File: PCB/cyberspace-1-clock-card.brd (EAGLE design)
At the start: 100 x 50 mm, 40 parts, among them U1 555, U2 Quad AND Gate, U3 Quad AND Gate, U4 QUAD NAND Gate, U5 SCHMIDT INVERTER, U6 HCT32, X1 1-14MHz

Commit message: Clock Card final?
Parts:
- added LOGO1: (no value), gfx-glyphs:SOZU-20MM
- added LOGO2: (no value), gfx-glyphs:CHRONOS2-20MM
- R13: value 1K -> 2K
- U2, U3: value Quad AND Gate -> HCT08
- U4: value QUAD NAND Gate -> HCT00
- U5: value SCHMIDT INVERTER -> HCT14
- moved R13 41.4 mm to (47.8, 37.0), turned to 90 degrees
- moved C4 10.7 mm to (32.7, 15.0)
- moved R12 10.7 mm to (54.3, 37.0)
- moved C5 10.1 mm to (52.9, 37.0)
- moved X1 5.21 mm to (55.0, 43.6), turned to 0 degrees
- moved C1 1.89 mm to (37.5, 25.4)
- moved C10 1.89 mm to (67.5, 25.4)
- moved C7 1.89 mm to (7.50, 25.4)
- moved C8 1.89 mm to (22.5, 25.4)
- moved C9 1.89 mm to (52.5, 25.4)
- moved U2 1.60 mm to (14.0, 25.4)
- moved U3 1.60 mm to (29.0, 25.4)
- moved U4 1.60 mm to (44.0, 25.4)
- moved U5 1.60 mm to (59.0, 25.4)
- moved U6 1.60 mm to (74.0, 25.4)
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- renumbered RP1 to SLOW_ADJ
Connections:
- net !CLK_OUT: now also R13.1; no longer CLK.K
- net N$11: now also CLK.K, R13.2; no longer CLK.A, R13.1
- net VCC: now also CLK.A; no longer R13.2
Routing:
- net VCC: track 0.00 -> 197.9 mm, vias 0 -> 17
- net !MODE_SLOW: track 0.00 -> 113.6 mm, vias 0 -> 3
- net !MODE_MAN: track 0.00 -> 103.2 mm, vias 0 -> 3
- net !MODE_FAST: track 0.00 -> 97.0 mm, vias 0 -> 3
- net !BTN_SLOW: track 0.00 -> 94.2 mm, vias 0 -> 2
- net !BTN_FAST: track 0.00 -> 89.4 mm, vias 0 -> 2
- net !BTN_MAN: track 0.00 -> 85.9 mm, vias 0 -> 2
- net CLK_IN_SLOW: track 0.00 -> 68.8 mm, vias 0 -> 1
- net CLK_OUT: track 0.00 -> 63.4 mm, vias 0 -> 2
- net N$11: track 0.00 -> 58.6 mm
- net N$5: track 0.00 -> 51.5 mm, vias 0 -> 1
- net CLK_OUT_MAN: track 0.00 -> 49.9 mm, vias 0 -> 2
- net CLK_IN_FAST: track 0.00 -> 48.7 mm, vias 0 -> 2
- net CLK_OUT_FAST: track 0.00 -> 47.4 mm, vias 0 -> 2
- net CLK_OUT_SLOW: track 0.00 -> 45.9 mm, vias 0 -> 2
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- added copper zone on layer 1, net GND
- added copper zone on layer 16, net GND
- added copper zone on layer 1, net VCC
- added copper zone on layer 16, net VCC
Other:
- board text added: "2023/12"
- board text added: "Circuit Monkey"
- board text added: "Design by"
- board text added: "Multi-Mode System Clock"
- board text added: "Rev. A"
- board text added: "TIME IS ON THE OTHER SIDE"

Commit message: Resistor missing value.
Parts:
- SLOW_ADJ: value (none) -> 1M
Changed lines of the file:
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@@
 <setting verticaltext="up"/>
 </settings>
-<grid distance="0.1" unitdist="mm" unit="mm" style="lines" multiple="1" display="yes" altdistance="5" altunitdist="mil" altunit="mil"/>
+<grid distance="1" unitdist="mm" unit="mm" style="lines" multiple="1" display="yes" altdistance="5" altunitdist="mil" altunit="mil"/>
 <layers>
 <layer number="1" name="Top" color="4" fill="1" visible="yes" active="yes"/>
@@
 <attribute name="VALUE" x="67.246" y="25.4" size="0.2" layer="27" rot="R270" align="center"/>
 </element>
-<element name="SLOW_ADJ" library="rlc" library_urn="urn:adsk.eagle:library:4192893" package="CERMET_MULTI_3006P_THD" package3d_urn="urn:adsk.eagle:package:42461647/1" value="" x="79" y="7.5" smashed="yes">
+<element name="SLOW_ADJ" library="rlc" library_urn="urn:adsk.eagle:library:4192893" package="CERMET_MULTI_3006P_THD" package3d_urn="urn:adsk.eagle:package:42461647/1" value="1M" x="79" y="7.5" smashed="yes">
 <attribute name="COST01" value="2.00" x="79" y="7.5" size="1.778" layer="27" display="off"/>
 <attribute name="COST10" value="1.70" x="79" y="7.5" size="1.778" layer="27" display="off"/>

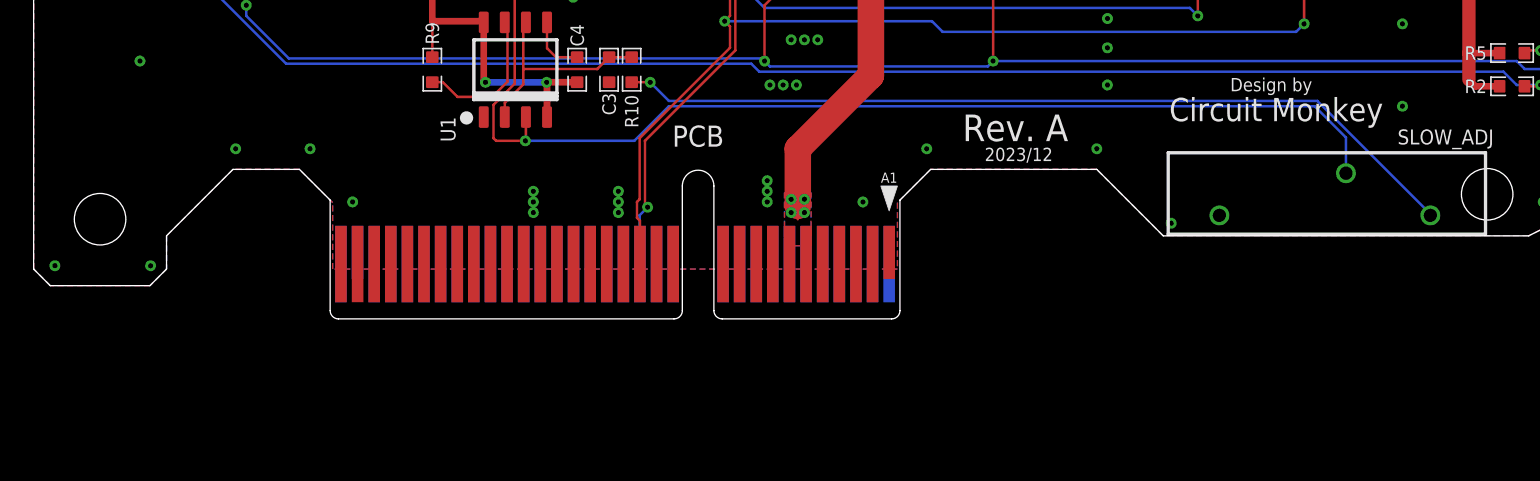
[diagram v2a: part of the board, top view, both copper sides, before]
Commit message: WIP. Proposed clock fix in schematic.
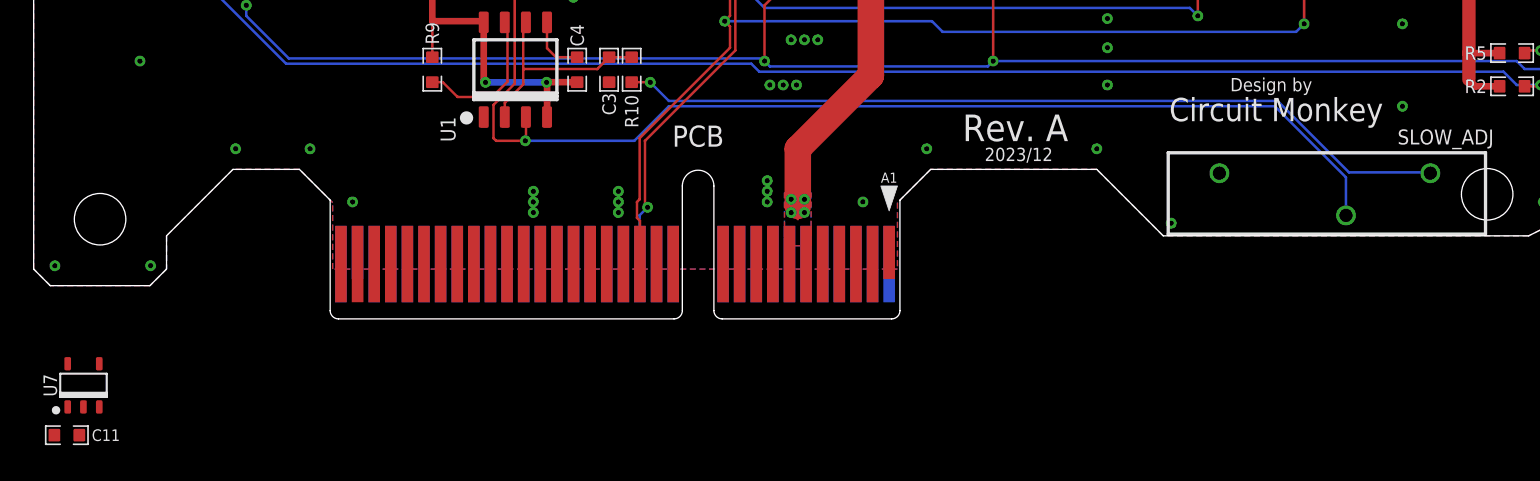
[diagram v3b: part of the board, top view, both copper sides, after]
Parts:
- added C11: 0.1uF, rlc:0603-CAP
- added U7: (no value), logic:TSOP-5
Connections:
- net GND: now also C11.2, U7.3
- net VCC: now also C11.1, U7.5
- net XTAL_IN: now also U7.2
- net XTAL_OUT: now also U7.4
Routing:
- net CLK_IN_SLOW: track 68.8 -> 69.9 mm
- net N$5: track 51.5 -> 50.3 mm
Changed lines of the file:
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@@
 <setting verticaltext="up"/>
 </settings>
-<grid distance="1" unitdist="mm" unit="mm" style="lines" multiple="1" display="yes" altdistance="5" altunitdist="mil" altunit="mil"/>
+<grid distance="0.1" unitdist="mm" unit="mm" style="lines" multiple="1" display="yes" altdistance="5" altunitdist="mil" altunit="mil"/>
 <layers>
 <layer number="1" name="Top" color="4" fill="1" visible="yes" active="yes"/>
@@
 <element name="LOGO1" library="gfx-glyphs" library_urn="urn:adsk.eagle:library:17868973" package="SOZU-20MM" value="" x="32.6" y="40" smashed="yes"/>
 <element name="LOGO2" library="gfx-glyphs" library_urn="urn:adsk.eagle:library:17868973" package="CHRONOS2-20MM" value="" x="73.1" y="38.4" smashed="yes"/>
+<element name="U7" library="logic" library_urn="urn:adsk.eagle:library:8032508" package="TSOP-5" package3d_urn="urn:adsk.eagle:package:8032592/3" value="" x="3" y="-4" smashed="yes">
+<attribute name="COST01" value="0.35" x="3" y="-4" size="1.778" layer="27" display="off"/>
+<attribute name="COST10" value="0.24" x="3" y="-4" size="1.778" layer="27" display="off"/>
+<attribute name="COST100" value="0.12" x="3" y="-4" size="1.778" layer="27" display="off"/>
+<attribute name="MFR" value="Nexperia" x="3" y="-4" size="1.778" layer="27" display="off"/>
+<attribute name="MPN" value="74HCT1G04GV" x="3" y="-4" size="1.778" layer="27" display="off"/>
+<attribute name="NAME" x="1" y="-4" size="0.8128" layer="25" font="vector" ratio="15" rot="R90" align="center"/>
+<attribute name="VALUE" x="3" y="-4" size="0.254" layer="27" font="vector" align="center"/>
+</element>
+<element name="C11" library="rlc" library_urn="urn:adsk.eagle:library:4192893" package="0603-CAP" package3d_urn="urn:adsk.eagle:package:4193021/5" value="0.1uF" x="2" y="-7" smashed="yes">
+<attribute name="COST01" value="0.12" x="2" y="-7" size="1.778" layer="27" display="off"/>
+<attribute name="COST10" value="0.09" x="2" y="-7" size="1.778" layer="27" display="off"/>
+<attribute name="COST100" value="0.05" x="2" y="-7" size="1.778" layer="27" display="off"/>
+<attribute name="NAME" x="3.5" y="-7" size="0.7" layer="25" font="vector" ratio="15" align="center-left"/>
+<attribute name="VALUE" x="2" y="-7.254" size="0.2" layer="27" align="center"/>
+</element>
 </elements>
 <signals>
@@
 <wire x1="52.5" y1="26.151840625" x2="51.351840625" y2="26.151840625" width="0.4" layer="1"/>
 <wire x1="51.351840625" y1="26.151840625" x2="51.2" y2="26" width="0.4" layer="1"/>
+<contactref element="U7" pad="5"/>
+<contactref element="C11" pad="1"/>
+<wire x1="2.05" y1="-2.7" x2="1.248159375" y2="-7" width="0" layer="19" extent="1-1"/>
+<wire x1="24" y1="15.751840625" x2="2.05" y2="-2.7" width="0" layer="19" extent="1-1"/>
 </signal>
 <signal name="GND">
@@
 <via x="64.64" y="16.32" extent="1-16" drill="0.3048"/>
 <via x="64.64" y="14.08" extent="1-16" drill="0.3048"/>
+<contactref element="U7" pad="3"/>
+<contactref element="C11" pad="2"/>
+<wire x1="2.751840625" y1="-7" x2="3.95" y2="-5.3" width="0" layer="19" extent="1-1"/>
+<wire x1="1.28" y1="3.2" x2="3.95" y2="-5.3" width="0" layer="19" extent="1-1"/>
 </signal>
 <signal name="XTAL_IN">
@@
 <wire x1="55.84" y1="32.96" x2="53.6" y2="35.2" width="0.1524" layer="1"/>
 <wire x1="52.9" y1="37.751840625" x2="53.6" y2="37.751840625" width="0.1524" layer="1"/>
+<contactref element="U7" pad="2"/>
+<wire x1="3" y1="-5.3" x2="59" y2="28.3" width="0" layer="19" extent="1-1"/>
 </signal>
 <signal name="XTAL_OUT">
@@
 <wire x1="56" y1="33.28" x2="57.44" y2="33.28" width="0.1524" layer="1"/>
 <wire x1="60.27" y1="28.3" x2="61.54" y2="28.3" width="0.1524" layer="1"/>
+<contactref element="U7" pad="4"/>
+<wire x1="3.95" y1="-2.7" x2="54.3" y2="36.248159375" width="0" layer="19" extent="1-1"/>
 </signal>
 <signal name="N$4">
@@
 <via x="29.6" y="10.72" extent="1-16" drill="0.3048"/>
 <wire x1="36.16" y1="10.72" x2="38.24" y2="12.8" width="0.1524" layer="16"/>
-<wire x1="38.24" y1="12.8" x2="77.12" y2="12.8" width="0.1524" layer="16"/>
+<wire x1="38.24" y1="12.8" x2="74.72" y2="12.8" width="0.1524" layer="16"/>
 <wire x1="29.6" y1="10.72" x2="36.16" y2="10.72" width="0.1524" layer="16"/>
-<wire x1="79" y1="8.77" x2="79" y2="10.92" width="0.1524" layer="16"/>
-<wire x1="79" y1="10.92" x2="77.12" y2="12.8" width="0.1524" layer="16"/>
+<wire x1="79" y1="6.23" x2="79" y2="8.52" width="0.1524" layer="16"/>
+<wire x1="79" y1="8.52" x2="74.72" y2="12.8" width="0.1524" layer="16"/>
 <wire x1="27.68" y1="10.88" x2="27.84" y2="10.72" width="0.1524" layer="1"/>
 <wire x1="27.84" y1="10.72" x2="29.6" y2="10.72" width="0.1524" layer="1"/>
@@
 <wire x1="37.111840625" y1="14.248159375" x2="37.12" y2="14.24" width="0.1524" layer="1"/>
 <via x="37.12" y="14.24" extent="1-16" drill="0.3048"/>
-<wire x1="84.08" y1="6.32" x2="77.28" y2="13.12" width="0.1524" layer="16"/>
+<wire x1="79.18" y1="8.82" x2="74.88" y2="13.12" width="0.1524" layer="16"/>
 <wire x1="37.12" y1="14.24" x2="38.24" y2="13.12" width="0.1524" layer="16"/>
-<wire x1="77.28" y1="13.12" x2="38.24" y2="13.12" width="0.1524" layer="16"/>
-<wire x1="84.08" y1="6.32" x2="84.08" y2="6.23" width="0.1524" layer="16"/>
+<wire x1="74.88" y1="13.12" x2="38.24" y2="13.12" width="0.1524" layer="16"/>
+<wire x1="84.03" y1="8.82" x2="79.18" y2="8.82" width="0.1524" layer="16"/>
+<wire x1="84.03" y1="8.82" x2="84.08" y2="8.77" width="0.1524" layer="16"/>
 </signal>
 <signal name="MODE_SLOW">
